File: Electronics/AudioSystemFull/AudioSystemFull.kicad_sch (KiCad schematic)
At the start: 292 parts, among them IC1 TDA1558Q, J1 SJ1-3515-SMT-TR-BE, J3 Conn_Display_Buttons, J6 Conn_ISO, U1 MIC39100-5.0WS, U10 LT3015EQ-5PBF, U11 OPA2134, U12 OPA2134, U13 OPA2134, U14 OPA2134, U15 OPA2134, U16 OPA2134, U17 OPA2134, U18 OPA2134, U19 OPA2134, U2 DEVKIT_V1_ESP32-WROOM-32, U20 OPA2134, U21 OPA2134, U22 OPA2134, U23 OPA2134, U24 OPA2134, U25 OPA2134, U26 OPA2134, U27 OPA2134, U28 OPA2134, U3 PCM5102A, U4 OPA2134, U5 LP5907MFX-3.3, U6 LMR51420YFDDCR, U7 LMR51420YFDDCR, U8 LP5907MFX-3.3, U9 LMR51420YFDDCR

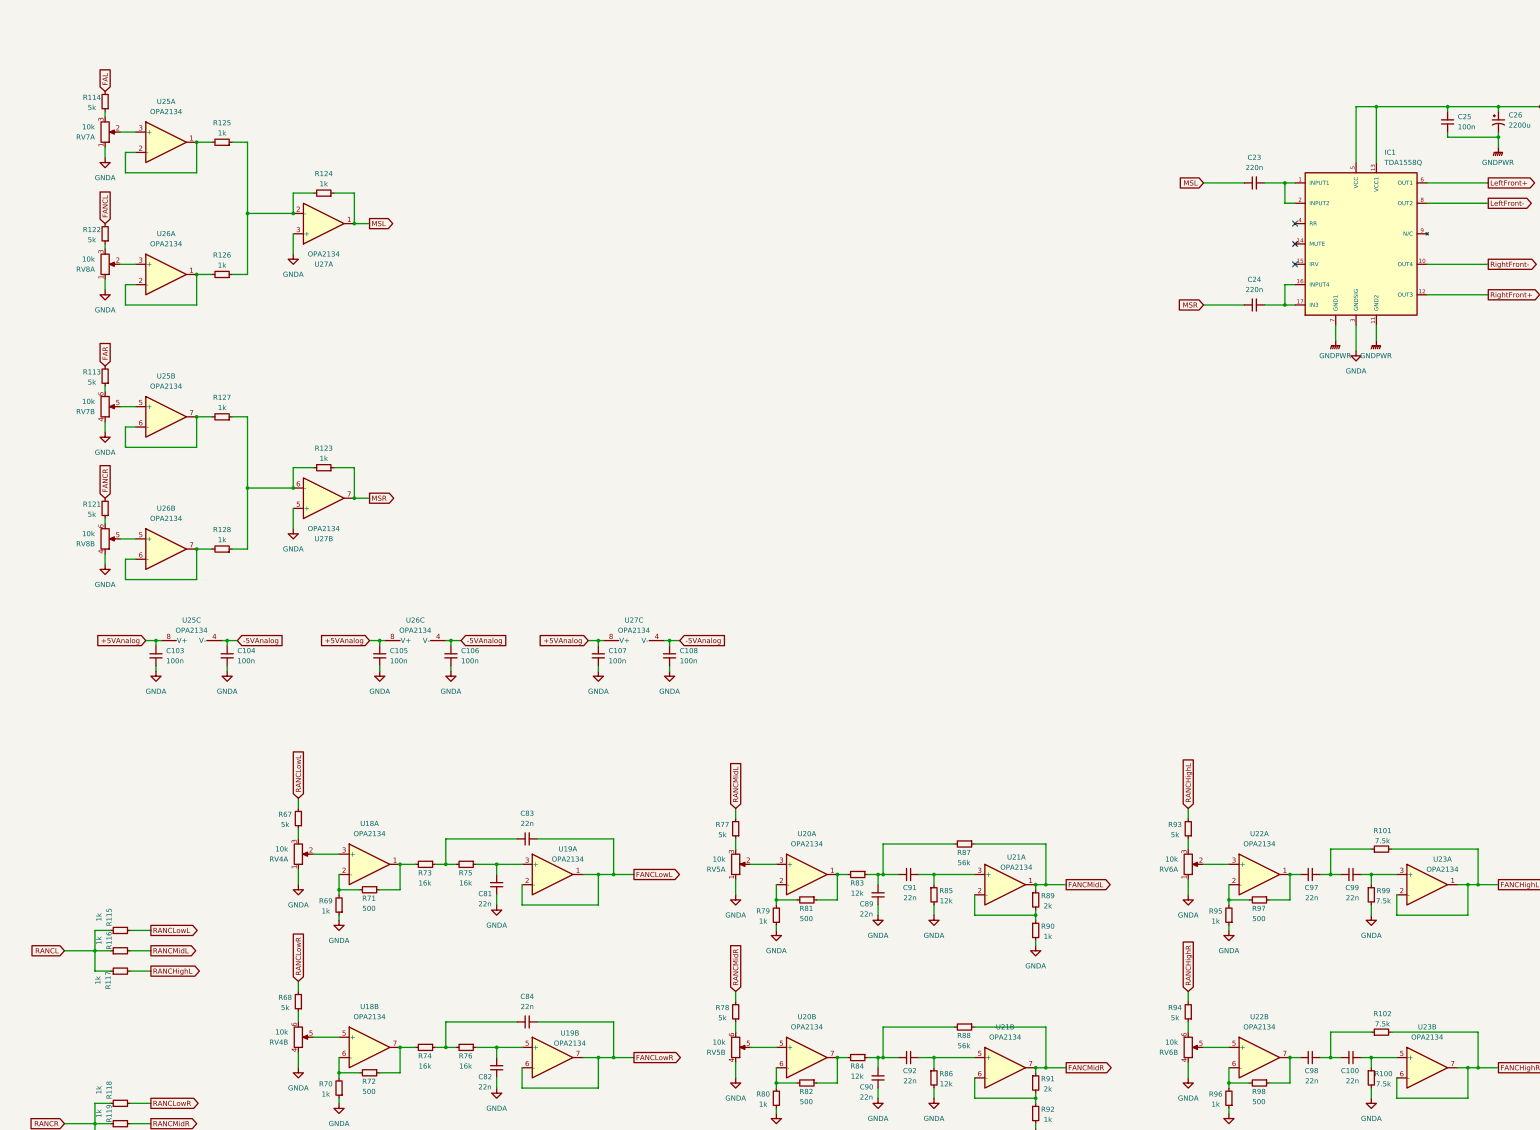
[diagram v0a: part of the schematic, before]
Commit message: add mounting holes to main pcb
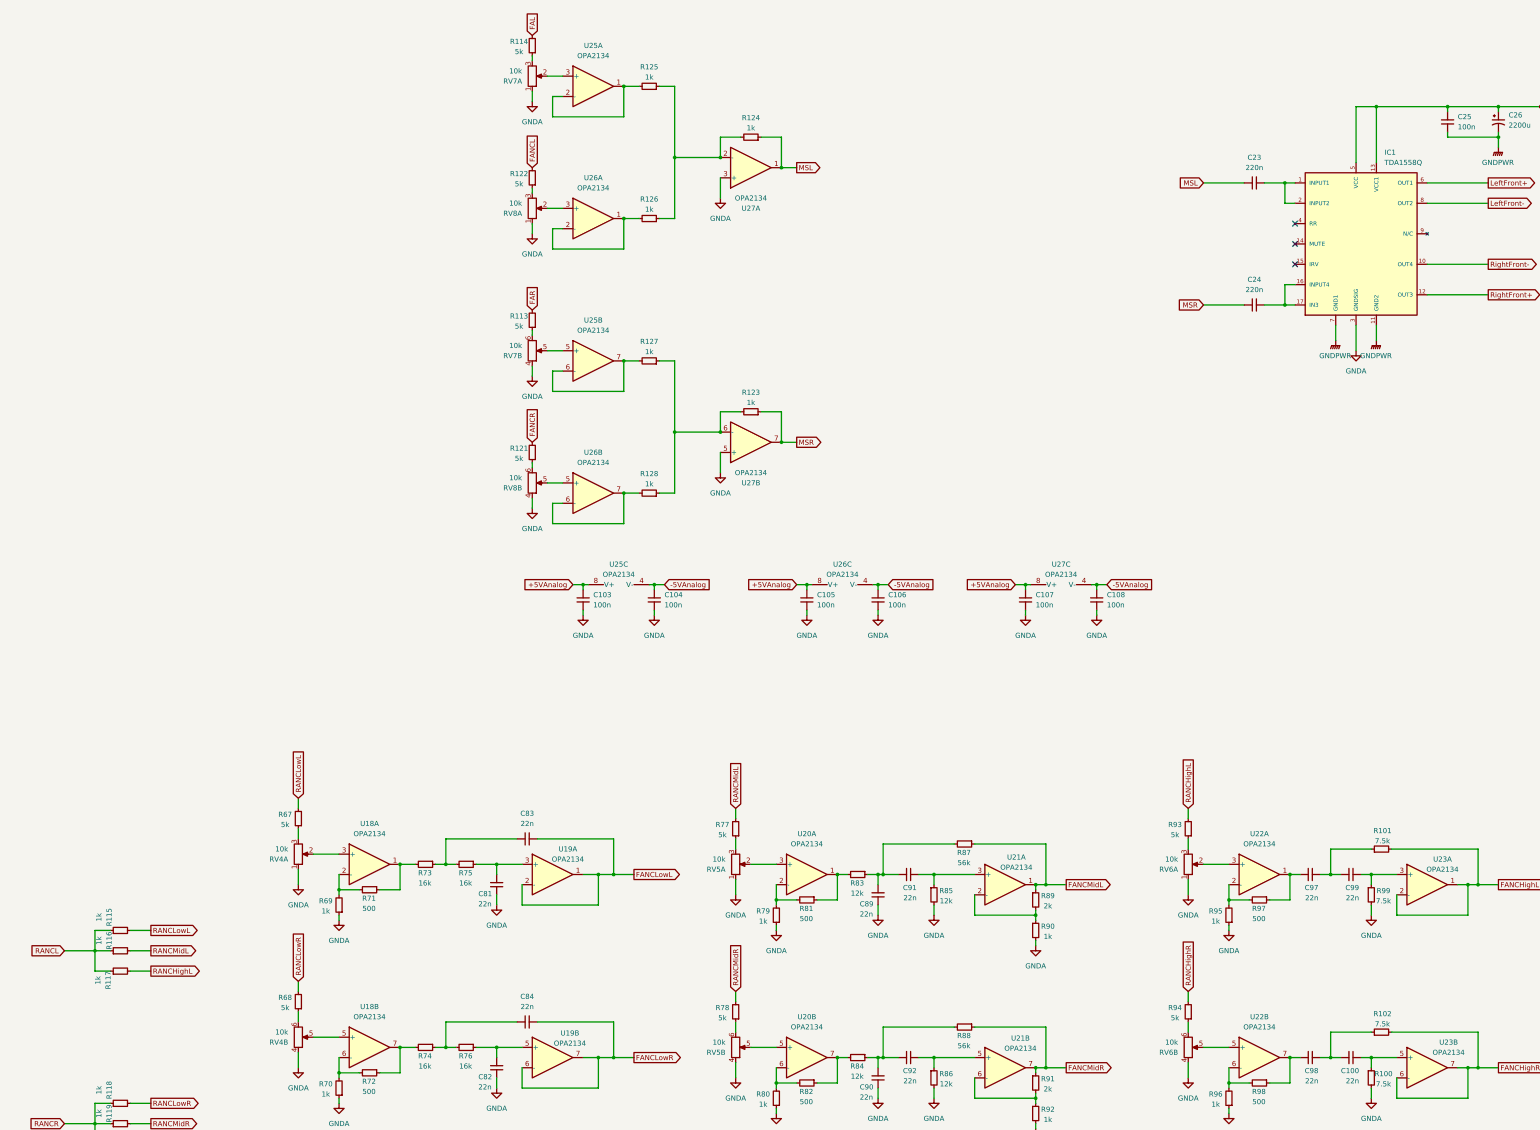
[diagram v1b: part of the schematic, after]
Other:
- moved on the sheet: C103, C104, C105, C106, C107, C108, R113, R114, R121, R122, R123, R124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

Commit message: bom
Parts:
- C1, C2: footprint Capacitor_SMD:C_0805_2012Metric_Pad1.18x1.45mm_HandSolder -> Capacitor_SMD:C_1206_3216Metric_Pad1.33x1.80mm_HandSolder; Check_prices (none) -> https://www.mouser.bg/ProductDetail/Murata-Electronics/GRM3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; Price (none) -> 1.19
- C10, C101, C102, C103, C104, C105, C106, C107, C108, C109, C110, C15, C16, C25, C30, C31, C33, C39, C44, C45, C47, C5, C6, C61, C62, C63, C64, C65, C66, C67, C68, C69, C70, C71, C72, C73, C74, C75, C76, C77, C78, C79, C8, C80, C85, C86, C87, C88, C93, C94, C95, C96: Check_prices (none) -> https://www.mouser.bg/ProductDetail/KEMET/C0805C104K3RACTU?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; MANUFACTURER_PART_NUMBER VJ1206Y104JXAAR -> C0805C104K3RACTU; Price (none) -> 0.186
- C100, C43, C50, C51, C52, C53, C54, C55, C56, C57, C58, C59, C60, C81, C82, C83, C84, C89, C90, C91, C92, C97, C98, C99: Check_prices (none) -> https://www.mouser.bg/ProductDetail/KEMET/C0805C223K5GEC721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; MANUFACTURER_PART_NUMBER CGA5C2NP01H223J060AA -> C0805C223K5GEC7210; Price (none) -> 0.559
- C11, C12, C20, C21, C3, C34, C35, C36, C4, C40, C41, C42: Check_prices (none) -> https://www.mouser.bg/ProductDetail/Murata-Electronics/GRM2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; MANUFACTURER_PART_NUMBER MCASU32MAB7106KPNA01 -> GRM21BZ71E106KE15K; Price (none) -> 0.541
- C111, C28, C37: Check_prices (none) -> https://www.mouser.bg/ProductDetail/Nichicon/UKT1V102MHD1TO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; Price (none) -> 1.71
- C13, C14: Check_prices (none) -> https://www.mouser.bg/ProductDetail/KEMET/C0805C222J5GACTU?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; MANUFACTURER_PART_NUMBER AC1206JRNPO9BN222 -> C0805C222J5GACTU; Price (none) -> 0.335
- C17, C29: Check_prices (none) -> https://www.mouser.bg/ProductDetail/KEMET/C0805C103K1RACTU?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; MANUFACTURER_PART_NUMBER C1206C103J1RACTU -> C0805C103K1RACTU; Price (none) -> 0.186
- C18, C19, C22, C27: Check_prices (none) -> https://www.mouser.bg/ProductDetail/80-C0805C105K3R?R=80-C0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; MANUFACTURER_PART_NUMBER C1206C105K3RAC7800 -> C0805C105K3RACTU; Price (none) -> 0.186
- C23, C24: footprint Capacitor_SMD:C_0805_2012Metric_Pad1.18x1.45mm_HandSolder -> Capacitor_SMD:C_1206_3216Metric_Pad1.33x1.80mm_HandSolder; Check_prices (none) -> https://www.mouser.bg/ProductDetail/Murata-Electronics/GRM3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; MANUFACTURER_PART_NUMBER GRM31C5C1H224JE02L -> GRM31C5C1E224JE02L; Price (none) -> 0.894
- C26: Check_prices (none) -> https://www.mouser.bg/ProductDetail/Chemi-Con/EGPD350ELL222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; Price (none) -> 4.61
- C32, C38, C46, C7, C9: Check_prices (none) -> https://www.mouser.bg/ProductDetail/YAGEO/CC0805KKX7R9BB225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; MANUFACTURER_PART_NUMBER GCJ31CR71H225KA12L -> CC0805KKX7R9BB225; Price (none) -> 0.67
- C48, C49: Check_prices (none) -> https://www.mouser.bg/ProductDetail/Murata-Electronics/GRM2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; MANUFACTURER_PART_NUMBER (none) -> GRM21BZ71E106KE15K; Price (none) -> 0.541
- IC1: Check_prices https://www.snapeda.com/parts/TDA1558Q/NXP+USA+Inc./view-pa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 -> (none)
- J1: Check_prices https://www.snapeda.com/parts/SJ1-3515-SMT-TR-BE/Same+Sky/v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 -> https://www.mouser.bg/ProductDetail/Same-Sky/SJ1-3515-SMT-T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; Price None -> 2.70
- J3: Check_prices (none) -> https://www.mouser.bg/ProductDetail/Molex/43045-1211?qs=359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; Price (none) -> 11.80
- J6, U3: Price (none) -> None
- L1, L3, L6: footprint AudioSystemFootprintLibrary:SRP0315-1R0K -> AudioSystemFootprintLibrary:SRP5030T-1R0M; Check_prices (none) -> https://www.mouser.bg/ProductDetail/Bourns/SRP5030T-1R0M?qs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; MANUFACTURER_PART_NUMBER SRP0315-1R0K -> SRP5030T-1R0M; Price (none) -> 2.39
- L2, L7: Check_prices (none) -> https://www.mouser.bg/ProductDetail/TDK/VLS6045EX-4R7M-H?qs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; MANUFACTURER_PART_NUMBER (none) -> VLS6045EX-4R7M-H; Price (none) -> 0.745
- L4: Check_prices (none) -> https://www.mouser.bg/ProductDetail/TDK/VLS6045EX-4R7M-H?qs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; Price (none) -> 0.745
- R1, R3: Check_prices (none) -> https://www.mouser.bg/ProductDetail/YAGEO/RT0805FRE10100KL?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; MANUFACTURER_PART_NUMBER (none) -> RT0805FRE10100KL; Price (none) -> 0.186
- R10, R15, R45: Check_prices (none) -> https://www.mouser.bg/ProductDetail/YAGEO/RT0805FRE10100KL?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; MANUFACTURER_PART_NUMBER RNCU1206BTE100K -> RT0805FRE10100KL; Price (none) -> 0.186
- R100, R101, R102, R55, R56, R57, R58, R99: Check_prices (none) -> https://www.mouser.bg/ProductDetail/YAGEO/RT0805FRE077K5L?q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; MANUFACTURER_PART_NUMBER RT1206FRE077K5L -> RT0805FRE077K5L; Price (none) -> 0.186
- R103, R104, R105, R106, R107, R108, R109, R11, R110, R115, R116, R117, R118, R119, R12, R120, R123, R124, R125, R126, R127, R128, R13, R14, R17, R18, R21, R23, R31, R33, R41, R48, R51, R53, R59, R60, R61, R62, R63, R64, R65, R66, R69, R70, R79, R80, R90, R92, R95, R96: Check_prices (none) -> https://www.mouser.bg/ProductDetail/YAGEO/RT0805FRE071KL?qs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; MANUFACTURER_PART_NUMBER RNCP1206FTD1K00 -> RT0805FRE071KL; Price (none) -> 0.186
- R111, R112, R5, R6: Check_prices (none) -> https://www.mouser.bg/ProductDetail/YAGEO/RT0805DRD07470RL?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; MANUFACTURER_PART_NUMBER RT1206DRE07470RL -> RT0805DRD07470RL; Price (none) -> 0.186
- R113, R114, R121, R122, R16, R20, R29, R30, R49, R50, R67, R68, R77, R78, R93, R94: Check_prices (none) -> https://www.mouser.bg/ProductDetail/Bourns/CRT0805-BY-5001E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; MANUFACTURER_PART_NUMBER RT1206BRD075KL -> CRT0805-BY-5001EAS; Price (none) -> 0.29
- R129, R130, R131, R132, R133, R8: Check_prices (none) -> https://www.mouser.bg/ProductDetail/YAGEO/PT0805-R-070RL?qs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; MANUFACTURER_PART_NUMBER HRG3216P-1800-D-T1 -> PT0805-R-070RL; Price (none) -> 0.819
- R134, R135: Check_prices (none) -> https://www.mouser.bg/ProductDetail/YAGEO/RT0805FRE1310KL?q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; MANUFACTURER_PART_NUMBER (none) -> RT0805FRE1310KL; Price (none) -> 0.186
- R19: Check_prices (none) -> https://www.mouser.bg/ProductDetail/YAGEO/RT0805FRE07110RL?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; MANUFACTURER_PART_NUMBER HRG3216P-1800-D-T1 -> RT0805FRE07110RL; Price (none) -> 0.186
- R2: Check_prices (none) -> https://www.mouser.bg/ProductDetail/YAGEO/RT0805FRE07240RL?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; MANUFACTURER_PART_NUMBER HRG3216P-2400-D-T1 -> RT0805FRE07240RL; Price (none) -> 0.186
- R22, R24, R32, R34, R52, R54, R71, R72, R81, R82, R97, R98: Check_prices (none) -> https://www.mouser.bg/ProductDetail/KOA-Speer/RN73R2ATTD500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; MANUFACTURER_PART_NUMBER RN73R2ATTD5000B25 -> RN73R2ATTD5000B25; Price (none) -> 0.355
- R25, R26, R27, R28, R73, R74, R75, R76: Check_prices (none) -> https://www.mouser.bg/ProductDetail/YAGEO/RT0805FRE0716KL?q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; MANUFACTURER_PART_NUMBER RT1206FRE0716KL -> RT0805FRE0716KL; Price (none) -> 0.186
- R35, R37, R38, R42, R83, R84, R85, R86: Check_prices (none) -> https://www.mouser.bg/ProductDetail/YAGEO/RT0805FRE0712KL?q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; MANUFACTURER_PART_NUMBER RT1206DRE0712KL -> RT0805FRE0712KL; Price (none) -> 0.186
- R36, R43, R87, R88: Check_prices (none) -> https://www.mouser.bg/ProductDetail/YAGEO/RT0805DRE0756KL?q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; MANUFACTURER_PART_NUMBER RT1206DRE0756KL -> RT0805DRE0756KL; Price (none) -> 0.186
- R39, R47, R89, R91: Check_prices (none) -> https://www.mouser.bg/ProductDetail/YAGEO/RT0805FRE102KL?qs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; MANUFACTURER_PART_NUMBER RT1206FRD072KL -> RT0805FRE102KL; Price (none) -> 0.186
- R4: Check_prices (none) -> https://www.mouser.bg/ProductDetail/YAGEO/RT0805FRE0711KL?q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; MANUFACTURER_PART_NUMBER HRG3216P-1102-D-T1 -> RT0805FRE0711KL; Price (none) -> 0.186
- R40, R44: Check_prices (none) -> https://www.mouser.bg/ProductDetail/YAGEO/RT0805BRD07320RL?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; MANUFACTURER_PART_NUMBER RN732BTTD3200F50 -> RT0805BRD07320RL; Price (none) -> 0.318
- R46: Check_prices (none) -> https://www.mouser.bg/ProductDetail/YAGEO/RT0805FRE0712KL?q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; MANUFACTURER_PART_NUMBER HRG3216P-1202-D-T1 -> RT0805FRE0712KL; Price (none) -> 0.186
- R7: Check_prices (none) -> https://www.mouser.bg/ProductDetail/YAGEO/RT0805FRE102KL?qs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; MANUFACTURER_PART_NUMBER (none) -> RT0805FRE102KL; Price (none) -> 0.186
- R9: Check_prices (none) -> https://www.mouser.bg/ProductDetail/YAGEO/RT0805FRE0711KL?q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; MANUFACTURER_PART_NUMBER RNCU1206BTE10K0 -> RT0805FRE0711KL; Price (none) -> 0.186
- RV1, RV2, RV3, RV4, RV5, RV6, RV7, RV8: Check_prices (none) -> https://www.mouser.bg/ProductDetail/Same-Sky/PTN092-H10120K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; Price (none) -> 3.29
- U1: Check_prices https://www.snapeda.com/parts/MIC39100-5.0WS-TR/Microchip/v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 -> https://www.mouser.bg/ProductDetail/Microchip-Technology/MI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; MANUFACTURER_PART_NUMBER (none) -> MIC39100-5.0WS-TR; Price None -> 3.53
- U10: Check_prices https://www.snapeda.com/parts/LT3015EQ-5%23PBF/Analog+Devic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 -> https://www.mouser.bg/ProductDetail/Analog-Devices/LT3015EQ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; Price None -> 16.17
- U11, U12, U13, U14, U15, U16, U17, U18, U19, U20, U21, U22, U23, U24, U25, U26, U27, U28, U4: Check_prices (none) -> https://www.mouser.bg/ProductDetail/Texas-Instruments/OPA21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; Price (none) -> 5.94
- U2: Check_prices https://www.snapeda.com/parts/DEVKIT%20V1%20ESP32-WROOM-32/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 -> (none)
- U5, U8: Check_prices (none) -> https://www.mouser.bg/ProductDetail/Texas-Instruments/LP590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; Price (none) -> 0.839
- U6, U9: Check_prices https://www.snapeda.com/parts/LMR51420YFDDCR/Texas+Instrume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 -> https://www.mouser.bg/ProductDetail/Texas-Instruments/LMR51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; MANUFACTURER_PART_NUMBER (none) -> LMR51420YFDDCR; Price None -> 2.18
- U7: Check_prices https://www.snapeda.com/parts/LMR51420YFDDCR/Texas+Instrume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 -> https://www.mouser.bg/ProductDetail/Texas-Instruments/LMR51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; Price None -> 2.18
